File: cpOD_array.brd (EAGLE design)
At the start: 128.3 x 106.7 mm, 177 parts, among them IC1X11 LM358D, IC1X12 LM358D, IC1X13 LM358D, IC1X21 LM358D, IC1X22 LM358D, IC1X23 LM358D, Q1X11 2N7002, Q1X12 2N7002, Q1X13 2N7002, Q1X21 2N7002, Q1X22 2N7002, Q1X23 2N7002

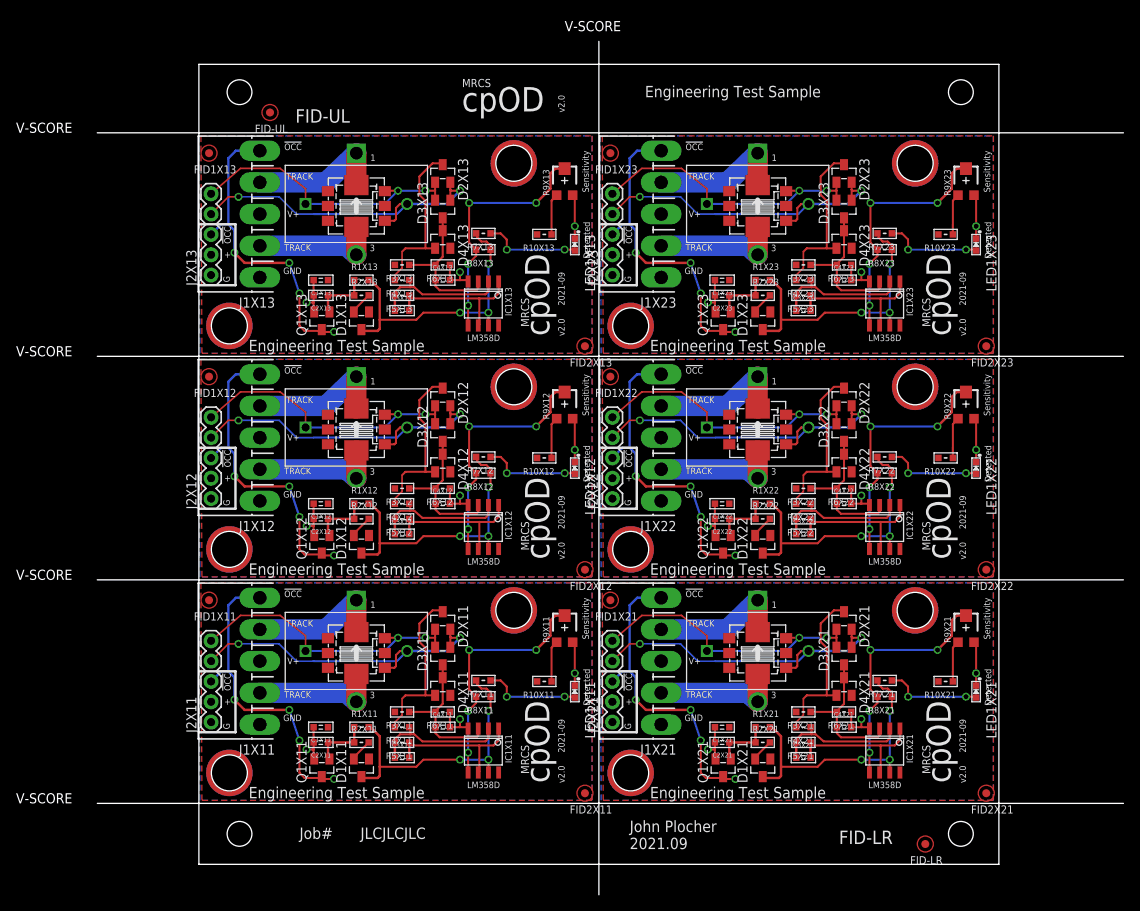
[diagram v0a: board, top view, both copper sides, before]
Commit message: LED1 shorted, D2/3 reversed
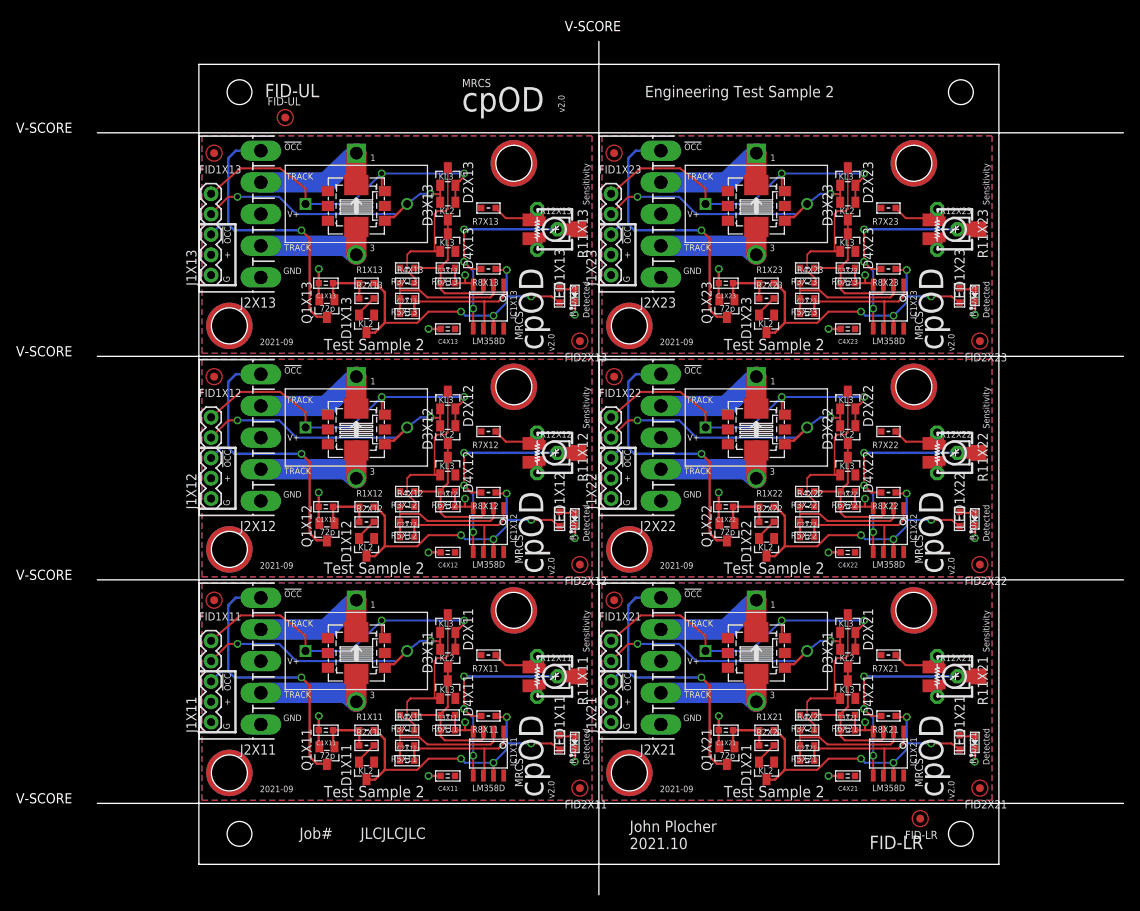
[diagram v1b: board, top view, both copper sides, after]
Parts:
- removed U$5X21, U$5X22, U$5X23, U$6X21, U$6X22, U$6X23: MOUNTINGHOLEL, SPCoast:MOUNTINGHOLE-L
- added R11X11, R11X12, R11X13, R11X21, R11X22, R11X23: 10K, SPCoast:PT-10S
- added R12X11, R12X12, R12X13, R12X21, R12X22, R12X23: 10K, SPCoast:TC33X
- added U$1X21, U$1X22, U$1X23, U$2X21, U$2X22, U$2X23: MOUNTINGHOLEL, SPCoast:MOUNTINGHOLE-L
- C1X11, C1X12, C1X13, C1X21, C1X22, C1X23: value 0.1uF -> 1.0uF
- C2X11, C2X12, C2X13, C2X21, C2X22, C2X23: value 1uF -> 0.01uF
- C3X11, C3X12, C3X13, C3X21, C3X22, C3X23: value 0.01uF -> 0.1uF
- D2X11, D2X12, D2X13, D2X21, D2X22, D2X23: value BAT54A -> BAT54C
- D3X11, D3X12, D3X13, D3X21, D3X22, D3X23: value BAT54C -> BAT54A
- J1X11, J1X12, J1X13, J1X21, J1X22, J1X23: device SPCoast:KK-156-5 -> SPCoast:1X05
- J2X11, J2X12, J2X13, J2X21, J2X22, J2X23: device SPCoast:1X05 -> SPCoast:KK-156-5
- R10X11, R10X12, R10X13, R10X21, R10X22, R10X23: value 10k -> 2k2
- R1X11, R1X12, R1X13, R1X21, R1X22, R1X23: value 2.2M -> 2M2
- R2X11, R2X12, R2X13, R2X21, R2X22, R2X23, R3X11, R3X12, R3X13, R3X21, R3X22, R3X23, R6X11, R6X12, R6X13, R6X21, R6X22, R6X23: value 10k -> 10K
- R7X11, R7X12, R7X13, R7X21, R7X22, R7X23: value 3.3k -> 10K
- R9X11, R9X12, R9X13, R9X21, R9X22, R9X23: value 10k -> 10K; device SPCoast:TC33X -> SPCoast:ST-4
- moved C2X12 11.0 mm to (26.0, 40.9), turned to 0 degrees
- moved C2X13 11.0 mm to (26.0, 68.8), turned to 0 degrees
- moved C2X11 11.0 mm to (26.0, 13.0), turned to 0 degrees
- moved C2X21 10.9 mm to (76.0, 13.0), turned to 0 degrees
- moved C2X22 10.9 mm to (76.0, 40.9), turned to 0 degrees
- moved C2X23 10.9 mm to (76.0, 68.8), turned to 0 degrees
- moved J1X22 9.86 mm to (51.5, 45.7)
- moved J1X23 9.86 mm to (51.5, 73.7)
- moved J1X21 9.86 mm to (51.5, 17.8)
- moved J2X12 9.84 mm to (7.75, 53.3)
- moved J2X13 9.84 mm to (7.75, 81.3)
- moved J2X11 9.84 mm to (7.75, 25.4)
- moved J1X12 9.76 mm to (1.52, 45.7)
- moved J1X13 9.76 mm to (1.52, 73.7)
- moved J1X11 9.76 mm to (1.52, 17.8)
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- renumbered U$5X11 to U$1X11, U$5X12 to U$1X12, U$5X13 to U$1X13, U$6X11 to U$2X11, U$6X12 to U$2X12, U$6X13 to U$2X13
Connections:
- net !VOUTX11: now also J1X11.3, J2X11.5; no longer J1X11.5, J2X11.3
- net !VOUTX12: now also J1X12.3, J2X12.5; no longer J1X12.5, J2X12.3
- net !VOUTX13: now also J1X13.3, J2X13.5; no longer J1X13.5, J2X13.3
- net !VOUTX21: now also J1X21.3, J2X21.5; no longer J1X21.5, J2X21.3
- net !VOUTX22: now also J1X22.3, J2X22.5; no longer J1X22.5, J2X22.3
- net !VOUTX23: now also J1X23.3, J2X23.5; no longer J1X23.5, J2X23.3
- net DCC-AX11: now also J2X11.2; no longer J1X11.2
- net DCC-AX12: now also J2X12.2; no longer J1X12.2
- net DCC-AX13: now also J2X13.2; no longer J1X13.2
- net DCC-AX21: now also J2X21.2; no longer J1X21.2
- net DCC-AX22: now also J2X22.2; no longer J1X22.2
- net DCC-AX23: now also J2X23.2; no longer J1X23.2
- net DCC-BX11: now also J2X11.4; no longer J1X11.4
- net DCC-BX12: now also J2X12.4; no longer J1X12.4
- net DCC-BX13: now also J2X13.4; no longer J1X13.4
- net DCC-BX21: now also J2X21.4; no longer J1X21.4
- net DCC-BX22: now also J2X22.4; no longer J1X22.4
- net DCC-BX23: now also J2X23.4; no longer J1X23.4
- net DETECTEDX11: now also R10X11.2; no longer R7X11.2
- net DETECTEDX12: now also R10X12.2; no longer R7X12.2
- net DETECTEDX13: now also R10X13.2; no longer R7X13.2
- net DETECTEDX21: now also R10X21.2; no longer R7X21.2
- net DETECTEDX22: now also R10X22.2; no longer R7X22.2
- net DETECTEDX23: now also R10X23.2; no longer R7X23.2
- net GNDX11: now also C3X11.2, R11X11.3, R12X11.2; no longer C2X11.2
- net GNDX12: now also C3X12.2, R11X12.3, R12X12.2; no longer C2X12.2
- net GNDX13: now also C3X13.2, R11X13.3, R12X13.2; no longer C2X13.2
- net GNDX21: now also C3X21.2, R11X21.3, R12X21.2; no longer C2X21.2
- net GNDX22: now also C3X22.2, R11X22.3, R12X22.2; no longer C2X22.2
- net GNDX23: now also C3X23.2, R11X23.3, R12X23.2; no longer C2X23.2
- net INPUT-AX11: now also D2X11.1, D3X11.2, J1X11.4; no longer D2X11.2, D3X11.1, J2X11.4
- net INPUT-AX12: now also D2X12.1, D3X12.2, J1X12.4; no longer D2X12.2, D3X12.1, J2X12.4
- net INPUT-AX13: now also D2X13.1, D3X13.2, J1X13.4; no longer D2X13.2, D3X13.1, J2X13.4
- net INPUT-AX21: now also D2X21.1, D3X21.2, J1X21.4; no longer D2X21.2, D3X21.1, J2X21.4
- net INPUT-AX22: now also D2X22.1, D3X22.2, J1X22.4; no longer D2X22.2, D3X22.1, J2X22.4
- net INPUT-AX23: now also D2X23.1, D3X23.2, J1X23.4; no longer D2X23.2, D3X23.1, J2X23.4
- net INPUT-BX11: now also D2X11.2, D3X11.1, J1X11.5; no longer D2X11.1, D3X11.2, J2X11.5
- net INPUT-BX12: now also D2X12.2, D3X12.1, J1X12.5; no longer D2X12.1, D3X12.2, J2X12.5
- net INPUT-BX13: now also D2X13.2, D3X13.1, J1X13.5; no longer D2X13.1, D3X13.2, J2X13.5
- net INPUT-BX21: now also D2X21.2, D3X21.1, J1X21.5; no longer D2X21.1, D3X21.2, J2X21.5
- net INPUT-BX22: now also D2X22.2, D3X22.1, J1X22.5; no longer D2X22.1, D3X22.2, J2X22.5
- net INPUT-BX23: now also D2X23.2, D3X23.1, J1X23.5; no longer D2X23.1, D3X23.2, J2X23.5
- net N$11X11: now also R10X11.1; no longer R7X11.1
- net N$11X12: now also R10X12.1; no longer R7X12.1
- net N$11X13: now also R10X13.1; no longer R7X13.1
- net N$11X21: now also R10X21.1; no longer R7X21.1
- net N$11X22: now also R10X22.1; no longer R7X22.1
- net N$11X23: now also R10X23.1; no longer R7X23.1
- net OCCUPIEDX11: now also C1X11.1; no longer C2X11.1
- net OCCUPIEDX12: now also C1X12.1; no longer C2X12.1
- net OCCUPIEDX13: now also C1X13.1; no longer C2X13.1
- net OCCUPIEDX21: now also C1X21.1; no longer C2X21.1
- net OCCUPIEDX22: now also C1X22.1; no longer C2X22.1
- net OCCUPIEDX23: now also C1X23.1; no longer C2X23.1
- net SENS+X11: now also R11X11.1, R12X11.1, R7X11.1; no longer R10X11.1
- net SENS+X12: now also R11X12.1, R12X12.1, R7X12.1; no longer R10X12.1
- net SENS+X13: now also R11X13.1, R12X13.1, R7X13.1; no longer R10X13.1
- net SENS+X21: now also R11X21.1, R12X21.1, R7X21.1; no longer R10X21.1
- net SENS+X22: now also R11X22.1, R12X22.1, R7X22.1; no longer R10X22.1
- net SENS+X23: now also R11X23.1, R12X23.1, R7X23.1; no longer R10X23.1
- net SENSITIVITYX11: now also R11X11.2, R12X11.3
- net SENSITIVITYX12: now also R11X12.2, R12X12.3
- net SENSITIVITYX13: now also R11X13.2, R12X13.3
- net SENSITIVITYX21: now also R11X21.2, R12X21.3
- net SENSITIVITYX22: now also R11X22.2, R12X22.3
- net SENSITIVITYX23: now also R11X23.2, R12X23.3
- net STAGE1+X11: now also C3X11.1; no longer C4X11.1
- net STAGE1+X12: now also C3X12.1; no longer C4X12.1
- net STAGE1+X13: now also C3X13.1; no longer C4X13.1
- net STAGE1+X21: now also C3X21.1; no longer C4X21.1
- net STAGE1+X22: now also C3X22.1; no longer C4X22.1
- net STAGE1+X23: now also C3X23.1; no longer C4X23.1
- net STAGE1-X11: now also C2X11.1; no longer C3X11.1
- net STAGE1-X12: now also C2X12.1; no longer C3X12.1
- net STAGE1-X13: now also C2X13.1; no longer C3X13.1
- net STAGE1-X21: now also C2X21.1; no longer C3X21.1
- net STAGE1-X22: now also C2X22.1; no longer C3X22.1
- net STAGE1-X23: now also C2X23.1; no longer C3X23.1
- net TRIGGEREDX11: now also C2X11.2; no longer C3X11.2
- net TRIGGEREDX12: now also C2X12.2; no longer C3X12.2
- net TRIGGEREDX13: now also C2X13.2; no longer C3X13.2
- net TRIGGEREDX21: now also C2X21.2; no longer C3X21.2
- net TRIGGEREDX22: now also C2X22.2; no longer C3X22.2
- net TRIGGEREDX23: now also C2X23.2; no longer C3X23.2
- net V+X11: now also C4X11.1, J1X11.2, J2X11.3, R7X11.2; no longer C1X11.1, J1X11.3, J2X11.2, R10X11.2
- net V+X12: now also C4X12.1, J1X12.2, J2X12.3, R7X12.2; no longer C1X12.1, J1X12.3, J2X12.2, R10X12.2
- net V+X13: now also C4X13.1, J1X13.2, J2X13.3, R7X13.2; no longer C1X13.1, J1X13.3, J2X13.2, R10X13.2
- net V+X21: now also C4X21.1, J1X21.2, J2X21.3, R7X21.2; no longer C1X21.1, J1X21.3, J2X21.2, R10X21.2
- net V+X22: now also C4X22.1, J1X22.2, J2X22.3, R7X22.2; no longer C1X22.1, J1X22.3, J2X22.2, R10X22.2
- net V+X23: now also C4X23.1, J1X23.2, J2X23.3, R7X23.2; no longer C1X23.1, J1X23.3, J2X23.2, R10X23.2
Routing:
- net N$11X23: track 12.1 -> 1.97 mm, vias 2 -> 0
- net N$11X13: track 12.1 -> 1.97 mm, vias 2 -> 0
- net N$11X22: track 12.1 -> 1.97 mm, vias 2 -> 0
- net N$11X21: track 12.1 -> 1.97 mm, vias 2 -> 0
- net N$11X12: track 12.1 -> 1.97 mm, vias 2 -> 0
- net N$11X11: track 12.1 -> 1.97 mm, vias 2 -> 0
- net INPUT-BX23: track 36.6 -> 43.6 mm
- net INPUT-BX22: track 36.6 -> 43.6 mm
- net INPUT-BX13: track 36.6 -> 43.6 mm
- net INPUT-BX21: track 36.6 -> 43.6 mm
- net INPUT-BX11: track 36.6 -> 43.6 mm
- net INPUT-BX12: track 36.6 -> 43.6 mm
- net INPUT-AX13: track 42.1 -> 37.6 mm
- net INPUT-AX12: track 42.1 -> 37.6 mm
- net INPUT-AX11: track 42.1 -> 37.6 mm
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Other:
- board text added: "72p"
- board text added: "Engineering Test Sample 2"
- board text added: "John Plocher 2021.10"
- board text added: "KL2"
- board text added: "KL3"
- board text added: "Test Sample 2"
- board text removed: "Engineering Test Sample"
- board text removed: "John Plocher 2021.09"

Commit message: Version 2.0
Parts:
- moved FID-UL 8.89 mm to (1.91, 93.3)
- moved FID-LR 7.62 mm to (97.8, 5.71)
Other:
- board text added: "2021-10"
- board text removed: "2021-09"
